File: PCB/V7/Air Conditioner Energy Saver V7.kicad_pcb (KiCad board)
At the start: 2 copper layers, 81 x 38 mm, 74 parts, among them J1 Conn_01x05_Male, J2 Conn_01x06_Male, J4 Conn_01x04_Male, J5 Conn_01x04_Male, P13 TestPoint, P16 TestPoint, P17 TestPoint, P2 TestPoint, P22 TestPoint, P23 TestPoint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

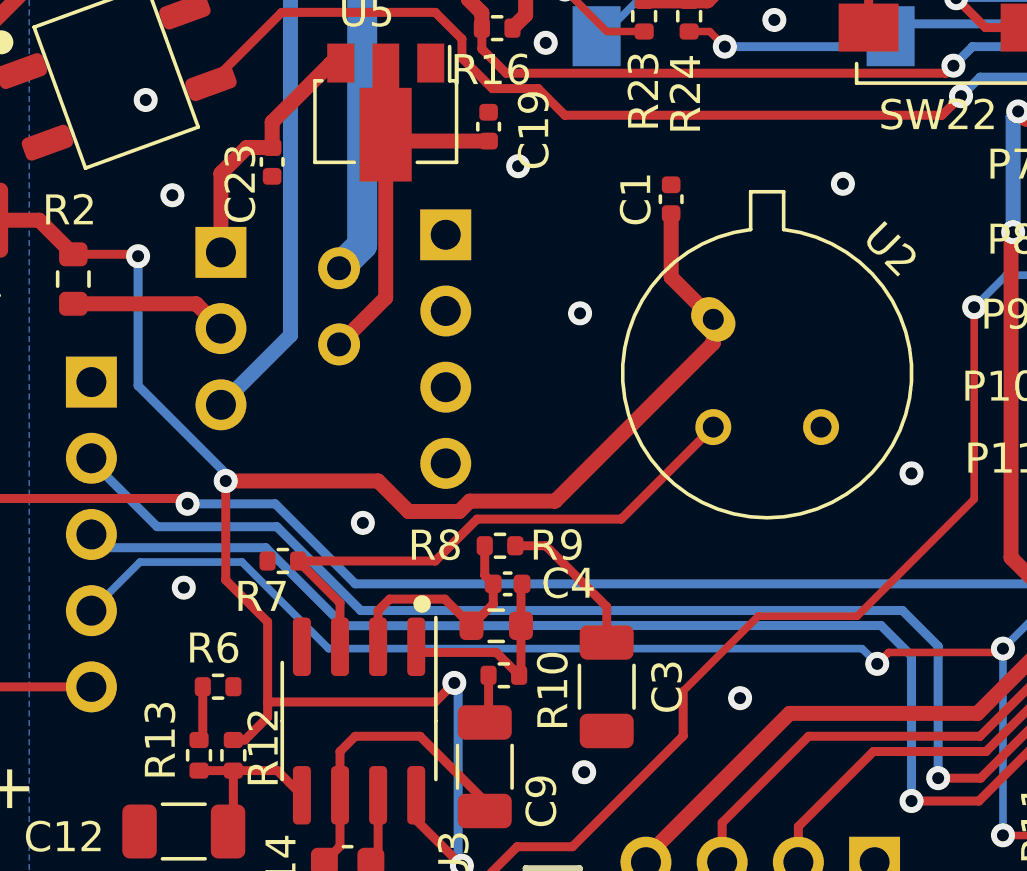
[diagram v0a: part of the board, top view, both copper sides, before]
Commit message: Updating to the latest V7 PCB that was submitted to JLCPCB
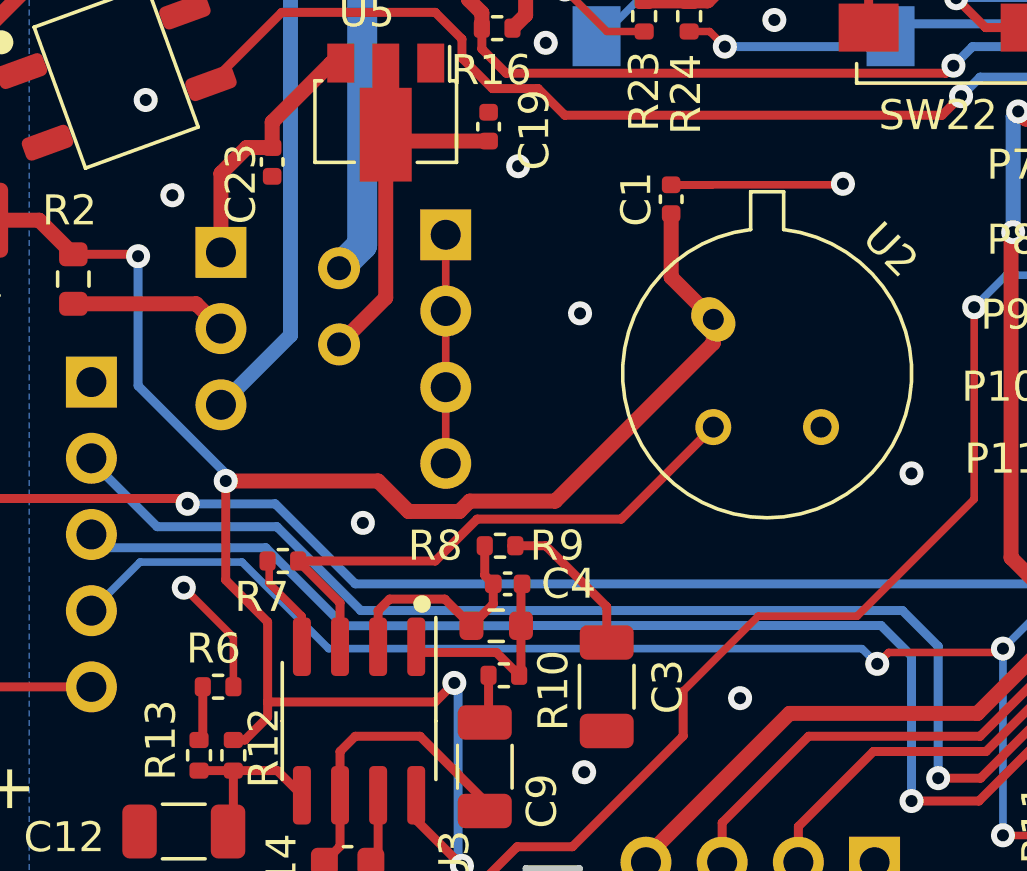
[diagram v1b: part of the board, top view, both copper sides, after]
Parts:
- removed the G*** at (125.9, 105.4)
- added G***: LOGO, Library_HD:QR_AC1, B.Cu at (126.0, 105.5)
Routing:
- net GND: track 6.61 -> 28.7 mm
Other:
- board text added: "June. 11, 2023"
- board text removed: "May. 30, 2023"
